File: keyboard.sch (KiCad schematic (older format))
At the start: 28 parts, among them CN2 KEYBOARD_HEADER, U13 MOS_6529, U20 74HCT273

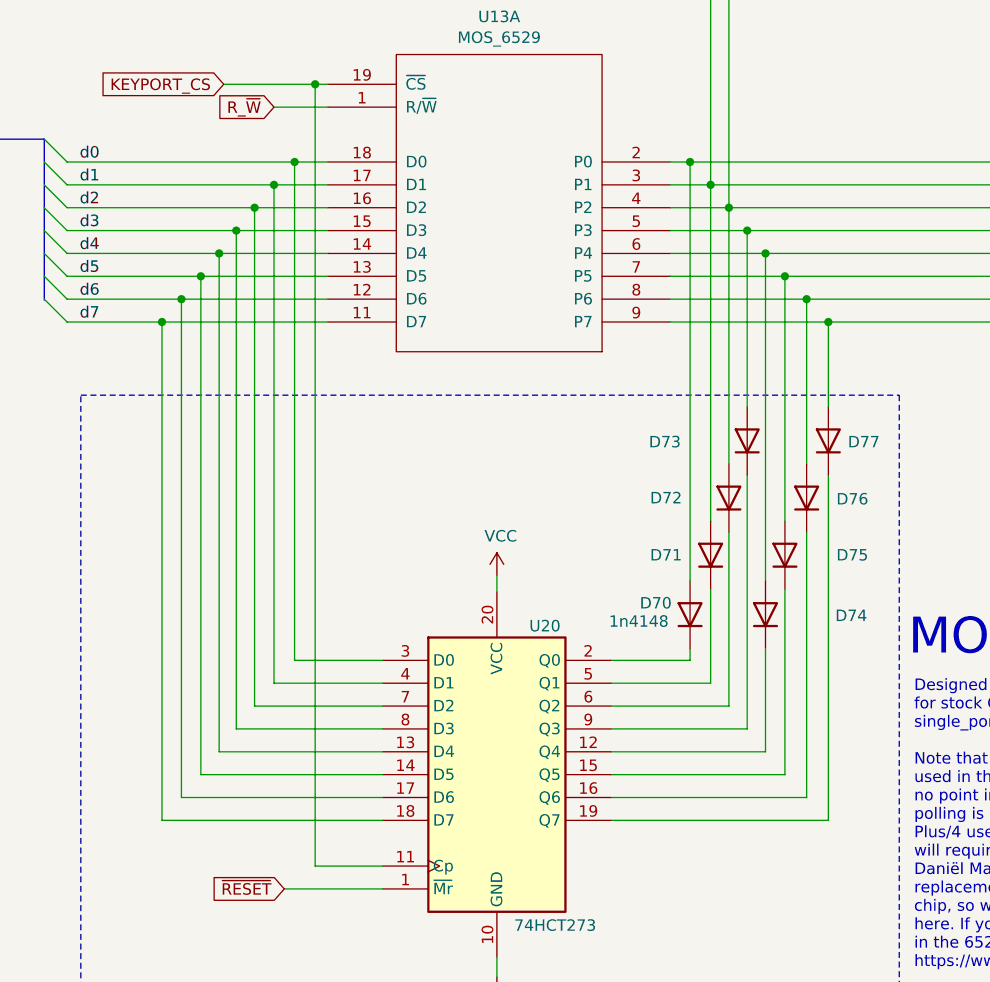
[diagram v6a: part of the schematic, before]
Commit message: Add working alternative for 6529 - Thanks @kinmami!
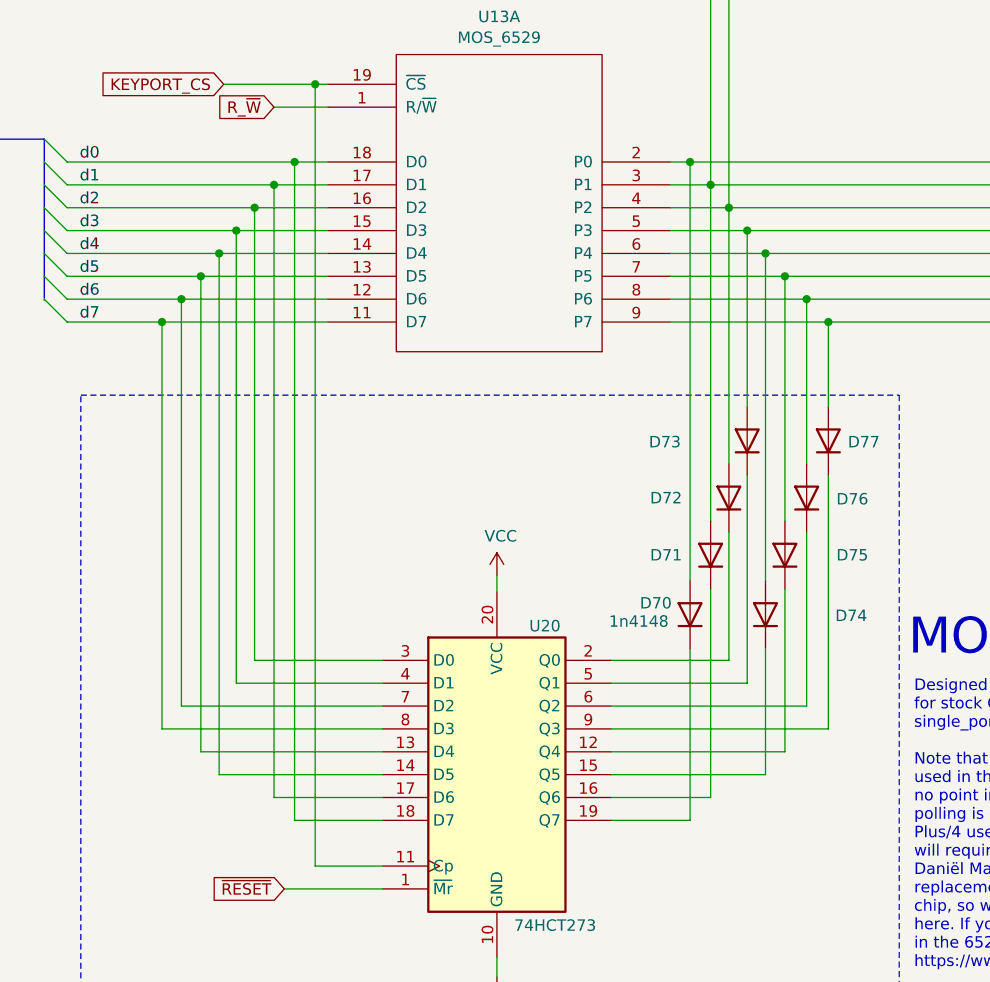
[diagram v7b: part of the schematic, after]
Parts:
- U20: footprint (none) -> LittleSixteen:DIP-20_W7.62mm_Socket_LongPads
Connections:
- net d0: now also U20.18 (D7); no longer U20.3 (D0)
- net d1: now also U20.17 (D6); no longer U20.4 (D1)
- net d2: now also U20.3 (D0); no longer U20.7 (D2)
- net d3: now also U20.4 (D1); no longer U20.8 (D3)
- net d4: now also U20.14 (D5); no longer U20.13 (D4)
- net d5: now also U20.13 (D4); no longer U20.14 (D5)
- net d6: now also U20.7 (D2); no longer U20.17 (D6)
- net d7: now also U20.8 (D3); no longer U20.18 (D7)
- net at U20.12 (Q4): now also D75.1 (K); no longer D74.1 (K)
- net at U20.15 (Q5): now also D74.1 (K); no longer D75.1 (K)
- net at U20.16 (Q6): now also D71.1 (K); no longer D76.1 (K)
- net at U20.19 (Q7): now also D70.1 (K); no longer D77.1 (K)
- net at U20.2 (Q0): now also D72.1 (K); no longer D70.1 (K)
- net at U20.5 (Q1): now also D73.1 (K); no longer D71.1 (K)
- net at U20.6 (Q2): now also D76.1 (K); no longer D72.1 (K)
- net at U20.9 (Q3): now also D77.1 (K); no longer D73.1 (K)
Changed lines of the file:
@@
 	6085 2315 6085 3435
 Wire Wire Line
-	6085 3735 6085 4495
-Wire Wire Line
-	5570 4495 6085 4495
-Wire Wire Line
-	5915 4295 5915 4245
+	6085 3735 6085 4295
 Wire Wire Line
 	5915 2115 5915 3945
 Wire Wire Line
 	6425 2715 6425 3435
-Wire Wire Line
-	6520 4995 6520 3485
-Wire Wire Line
-	5570 4995 6520 4995
-Wire Wire Line
-	6425 4895 5570 4895
-Wire Wire Line
-	5570 4795 6330 4795
-Wire Wire Line
-	6245 4695 5570 4695
-Wire Wire Line
-	5570 4595 6165 4595
 Wire Wire Line
 	5070 5680 5070 5595
@@
 $EndComp
 Wire Wire Line
-	3605 4995 3605 2815
-Wire Wire Line
-	4570 4995 3605 4995
-Wire Wire Line
-	3690 4895 4570 4895
-Wire Wire Line
-	3690 2715 3690 4895
-Wire Wire Line
-	3775 4795 3775 2615
-Wire Wire Line
-	4570 4795 3775 4795
-Wire Wire Line
-	3855 4695 4570 4695
-Wire Wire Line
-	3855 2515 3855 4695
-Wire Wire Line
-	3930 4595 3930 2415
-Wire Wire Line
-	4570 4595 3930 4595
-Wire Wire Line
-	4010 4495 4570 4495
-Wire Wire Line
-	4010 2315 4010 4495
-Wire Wire Line
-	4095 4395 4095 2215
-Wire Wire Line
-	4570 4395 4095 4395
-Wire Wire Line
-	4185 4295 4570 4295
-Wire Wire Line
-	4185 2115 4185 4295
+	3690 2715 3690 4495
 Text GLabel 4140 5295 0    50   Input ~ 0
 ~RESET
@@
 	0    -1   -1   0
 $EndComp
-Wire Wire Line
-	6005 3985 6005 4395
 $Comp
 L Device:D D71
@@
 	4275 1775 4275 5195
 Wire Wire Line
-	6005 4395 5570 4395
-Wire Wire Line
 	6005 2215 6005 3685
 Wire Wire Line
-	5570 4295 5915 4295
-Wire Wire Line
 	6330 2615 6330 3685
 Wire Wire Line
 	6245 2515 6245 3945
-Wire Wire Line
-	6165 4595 6165 3485
 $Comp
 L Device:D D73
@@
 	0    -1   -1   0
 $EndComp
-Wire Wire Line
-	6245 4245 6245 4695
 $Comp
 L Device:D D75
@@
 $EndComp
 Wire Wire Line
-	6330 3985 6330 4795
+	6330 3985 6330 4695
 $Comp
 L Device:D D76
@@
 $EndComp
 Wire Wire Line
-	6425 3735 6425 4895
+	6425 3735 6425 4495
 $Comp
 L Device:D D77
@@
 F 0 "U20" H 5280 5445 50  0000 C CNN
 F 1 "74HCT273" H 5325 4135 50  0000 C CNN
-F 2 "" H 5070 4795 50  0001 C CNN
+F 2 "LittleSixteen:DIP-20_W7.62mm_Socket_LongPads" H 5070 4795 50  0001 C CNN
 F 3 "https://assets.nexperia.com/documents/data-sheet/74HC_HCT273.pdf" H 5070 4795 50  0001 C CNN
 	1    5070 4795
@@
 Text Notes 6870 4290 0    157  ~ 0
 MOS6529 REPLACEMENT
+Wire Wire Line
+	4010 2315 4010 4295
+Wire Wire Line
+	3775 4695 3775 2615
+Wire Wire Line
+	3855 4795 4570 4795
+Wire Wire Line
+	3855 2515 3855 4795
+Wire Wire Line
+	3775 4695 4570 4695
+Wire Wire Line
+	4570 4395 3930 4395
+Wire Wire Line
+	3930 4395 3930 2415
+Wire Wire Line
+	4185 4995 4570 4995
+Wire Wire Line
+	4185 2115 4185 4995
+Wire Wire Line
+	4570 4295 4010 4295
+Wire Wire Line
+	4570 4595 3605 4595
+Wire Wire Line
+	3605 2815 3605 4595
+Wire Wire Line
+	4095 4895 4570 4895
+Wire Wire Line
+	4095 2215 4095 4895
+Wire Wire Line
+	4570 4495 3690 4495
+Wire Wire Line
+	5915 4995 5570 4995
+Wire Wire Line
+	5915 4245 5915 4995
+Wire Wire Line
+	6005 4895 5570 4895
+Wire Wire Line
+	6005 3985 6005 4895
+Wire Wire Line
+	5570 4295 6085 4295
+Wire Wire Line
+	5570 4395 6165 4395
+Wire Wire Line
+	6165 4395 6165 3485
+Wire Wire Line
+	5570 4795 6245 4795
+Wire Wire Line
+	6245 4245 6245 4795
+Wire Wire Line
+	5570 4695 6330 4695
+Wire Wire Line
+	5570 4495 6425 4495
+Wire Wire Line
+	5570 4595 6520 4595
+Wire Wire Line
+	6520 4595 6520 3485
 Wire Bus Line
 	3090 2015 3090 2720
